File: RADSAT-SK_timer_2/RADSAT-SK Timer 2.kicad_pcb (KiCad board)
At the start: 2 copper layers, 90.2 x 95.9 mm, 70 parts, among them J201 Conn_01x07, J202 Conn_01x05_Female, J203 Conn_01x03, J204 Conn_01x02, J205 Conn_01x02, J206 Conn_01x02, J207 Conn_02x26_Odd_Even, J208 Conn_02x26_Odd_Even, Q204 IRLML2060, Q205 IRLML2060, Q206 IRLML2060, SW201 SW_Push, SW202 SW_Push, SW203 SW_Push, SW204 SW_Push, SW205 SW_Push, SW206 SW_Push, U101 LT1521, U102 Galaxia_Timer, U202 TPS3700DDCR, U230 CPC1114N, U240 CPC1114N, U250 CPC1114N, U260 CPC1114N

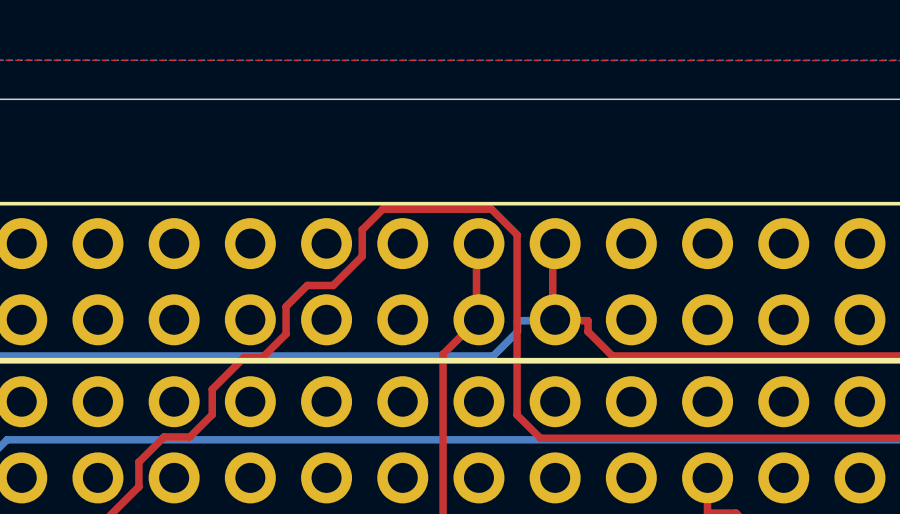
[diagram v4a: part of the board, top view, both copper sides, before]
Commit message: corrected I2C CSKB trace
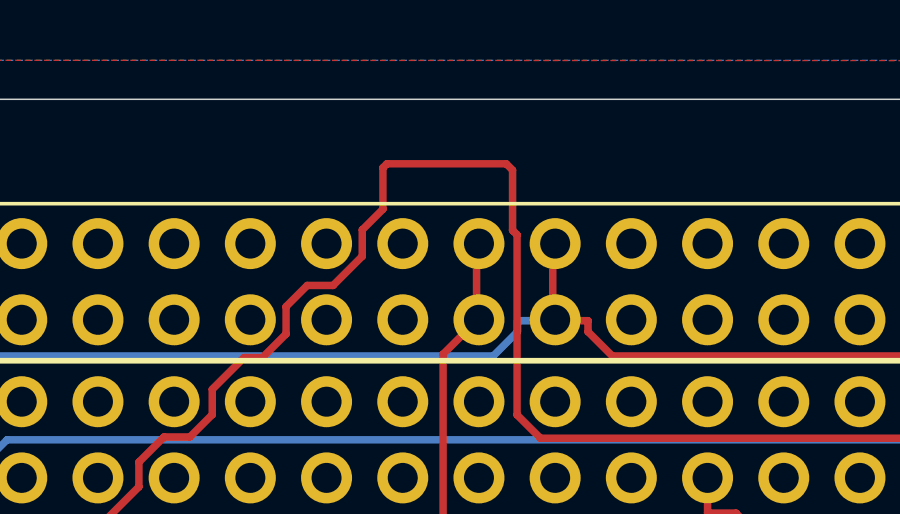
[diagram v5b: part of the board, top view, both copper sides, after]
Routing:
- net I2C_DATA: track 76.4 -> 79.6 mm
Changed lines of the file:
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@@
     (thickness 1.6)
     (drawings 233)
-    (tracks 416)
+    (tracks 421)
     (zones 0)
     (modules 70)
@@
   (segment (start 39.41 71.32) (end 53.0747 71.32) (width 0.25) (layer F.Cu) (net 1))
   (segment (start 53.0747 71.32) (end 53.2747 71.12) (width 0.25) (layer F.Cu) (net 1))
+  (segment (start 80.63 54.5165) (end 80.63 60.5183) (width 0.25) (layer F.Cu) (net 2))
+  (segment (start 80.63 60.5183) (end 81.4097 61.298) (width 0.25) (layer F.Cu) (net 2))
+  (segment (start 81.4097 61.298) (end 98.462 61.298) (width 0.25) (layer F.Cu) (net 2))
+  (segment (start 98.462 61.298) (end 99.68 60.08) (width 0.25) (layer F.Cu) (net 2))
+  (segment (start 56.6674 70.19) (end 57.28 70.19) (width 0.25) (layer F.Cu) (net 2))
+  (segment (start 56.6674 70.19) (end 56.0547 70.19) (width 0.25) (layer F.Cu) (net 2))
+  (segment (start 39.41 70.07) (end 55.9347 70.07) (width 0.25) (layer F.Cu) (net 2))
+  (segment (start 55.9347 70.07) (end 56.0547 70.19) (width 0.25) (layer F.Cu) (net 2))
+  (segment (start 80.27 52.15) (end 80.48 52.36) (width 0.25) (layer F.Cu) (net 2))
+  (segment (start 76.2892 52.15) (end 80.27 52.15) (width 0.25) (layer F.Cu) (net 2))
+  (segment (start 76.1596 52.2796) (end 76.2892 52.15) (width 0.25) (layer F.Cu) (net 2))
+  (segment (start 76.1596 53.6616) (end 76.1596 52.2796) (width 0.25) (layer F.Cu) (net 2))
+  (segment (start 75.47 54.3512) (end 76.1596 53.6616) (width 0.25) (layer F.Cu) (net 2))
+  (segment (start 75.47 55.2342) (end 75.47 54.3512) (width 0.25) (layer F.Cu) (net 2))
+  (segment (start 74.4996 56.2046) (end 75.47 55.2342) (width 0.25) (layer F.Cu) (net 2))
+  (segment (start 72.93 56.9124) (end 73.6378 56.2046) (width 0.25) (layer F.Cu) (net 2))
+  (segment (start 80.52675 54.41325) (end 80.63 54.5165) (width 0.25) (layer F.Cu) (net 2))
+  (segment (start 80.48 52.36) (end 80.48 54.3665) (width 0.25) (layer F.Cu) (net 2))
   (segment (start 57.28 70.19) (end 60.7524 70.19) (width 0.25) (layer F.Cu) (net 2))
+  (segment (start 80.48 54.3665) (end 80.52675 54.41325) (width 0.25) (layer F.Cu) (net 2))
+  (segment (start 73.6378 56.2046) (end 74.4996 56.2046) (width 0.25) (layer F.Cu) (net 2))
   (segment (start 60.7524 70.19) (end 68.0246 62.9178) (width 0.25) (layer F.Cu) (net 2))
+  (segment (start 70.47 60.511) (end 70.47 59.669) (width 0.25) (layer F.Cu) (net 2))
   (segment (start 68.0246 62.9178) (end 68.0246 62.0944) (width 0.25) (layer F.Cu) (net 2))
   (segment (start 68.0246 62.0944) (end 68.8636 61.2554) (width 0.25) (layer F.Cu) (net 2))
   (segment (start 68.8636 61.2554) (end 69.7256 61.2554) (width 0.25) (layer F.Cu) (net 2))
   (segment (start 69.7256 61.2554) (end 70.47 60.511) (width 0.25) (layer F.Cu) (net 2))
-  (segment (start 70.47 60.511) (end 70.47 59.669) (width 0.25) (layer F.Cu) (net 2))
   (segment (start 70.47 59.669) (end 71.528 58.611) (width 0.25) (layer F.Cu) (net 2))
   (segment (start 71.528 58.611) (end 72.1415 58.611) (width 0.25) (layer F.Cu) (net 2))
   (segment (start 72.1415 58.611) (end 72.93 57.8225) (width 0.25) (layer F.Cu) (net 2))
   (segment (start 72.93 57.8225) (end 72.93 56.9124) (width 0.25) (layer F.Cu) (net 2))
-  (segment (start 72.93 56.9124) (end 73.6378 56.2046) (width 0.25) (layer F.Cu) (net 2))
-  (segment (start 73.6378 56.2046) (end 74.4996 56.2046) (width 0.25) (layer F.Cu) (net 2))
-  (segment (start 74.4996 56.2046) (end 75.47 55.2342) (width 0.25) (layer F.Cu) (net 2))
-  (segment (start 75.47 55.2342) (end 75.47 54.3512) (width 0.25) (layer F.Cu) (net 2))
-  (segment (start 75.47 54.3512) (end 76.1596 53.6616) (width 0.25) (layer F.Cu) (net 2))
-  (segment (start 76.1596 53.6616) (end 79.7751 53.6616) (width 0.25) (layer F.Cu) (net 2))
-  (segment (start 79.7751 53.6616) (end 80.63 54.5165) (width 0.25) (layer F.Cu) (net 2))
-  (segment (start 80.63 54.5165) (end 80.63 60.5183) (width 0.25) (layer F.Cu) (net 2))
-  (segment (start 80.63 60.5183) (end 81.4097 61.298) (width 0.25) (layer F.Cu) (net 2))
-  (segment (start 81.4097 61.298) (end 98.462 61.298) (width 0.25) (layer F.Cu) (net 2))
-  (segment (start 98.462 61.298) (end 99.68 60.08) (width 0.25) (layer F.Cu) (net 2))
-  (segment (start 56.6674 70.19) (end 57.28 70.19) (width 0.25) (layer F.Cu) (net 2))
-  (segment (start 56.6674 70.19) (end 56.0547 70.19) (width 0.25) (layer F.Cu) (net 2))
-  (segment (start 39.41 70.07) (end 55.9347 70.07) (width 0.25) (layer F.Cu) (net 2))
-  (segment (start 55.9347 70.07) (end 56.0547 70.19) (width 0.25) (layer F.Cu) (net 2))
   (segment (start 119.708 97.4) (end 117.186 97.4) (width 0.25) (layer F.Cu) (net 4))
   (segment (start 117.186 97.4) (end 116.288 98.298) (width 0.25) (layer F.Cu) (net 4))

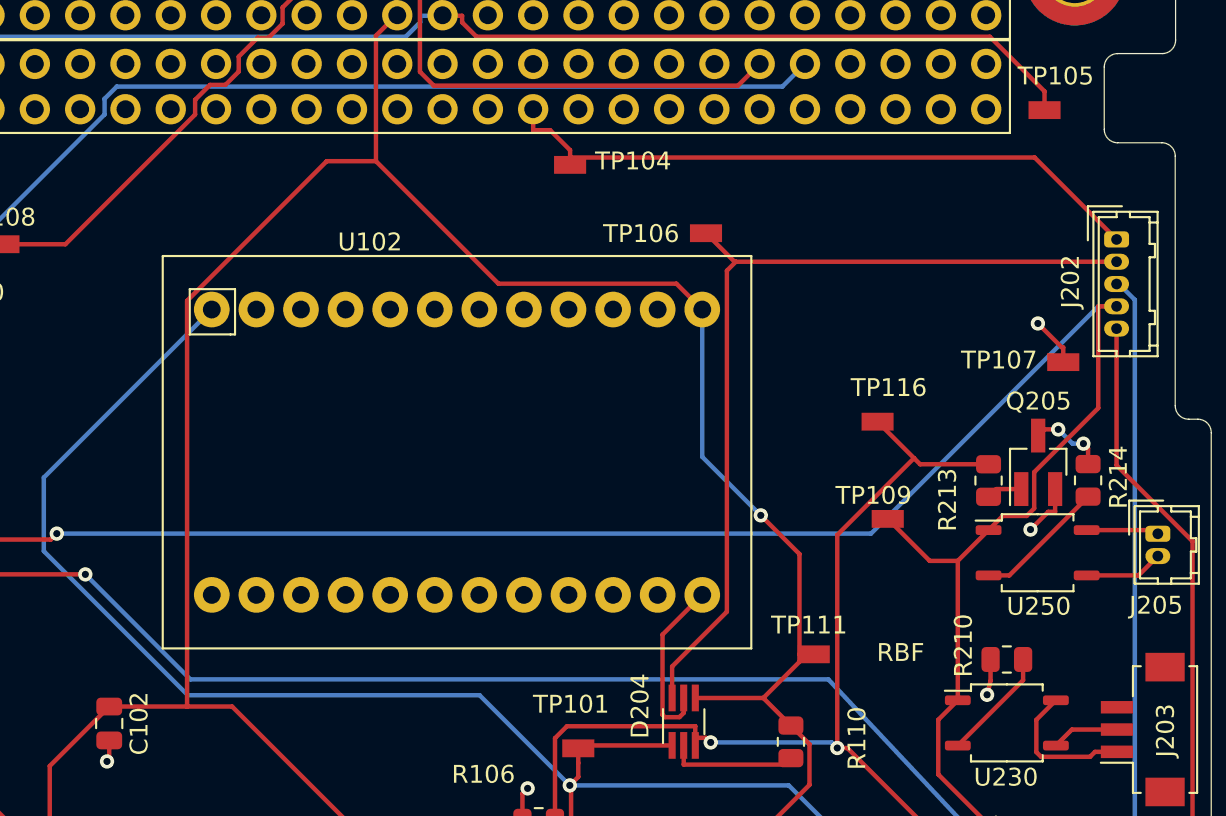
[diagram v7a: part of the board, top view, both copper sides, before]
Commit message: gave traces breathing room along the galaxia timer
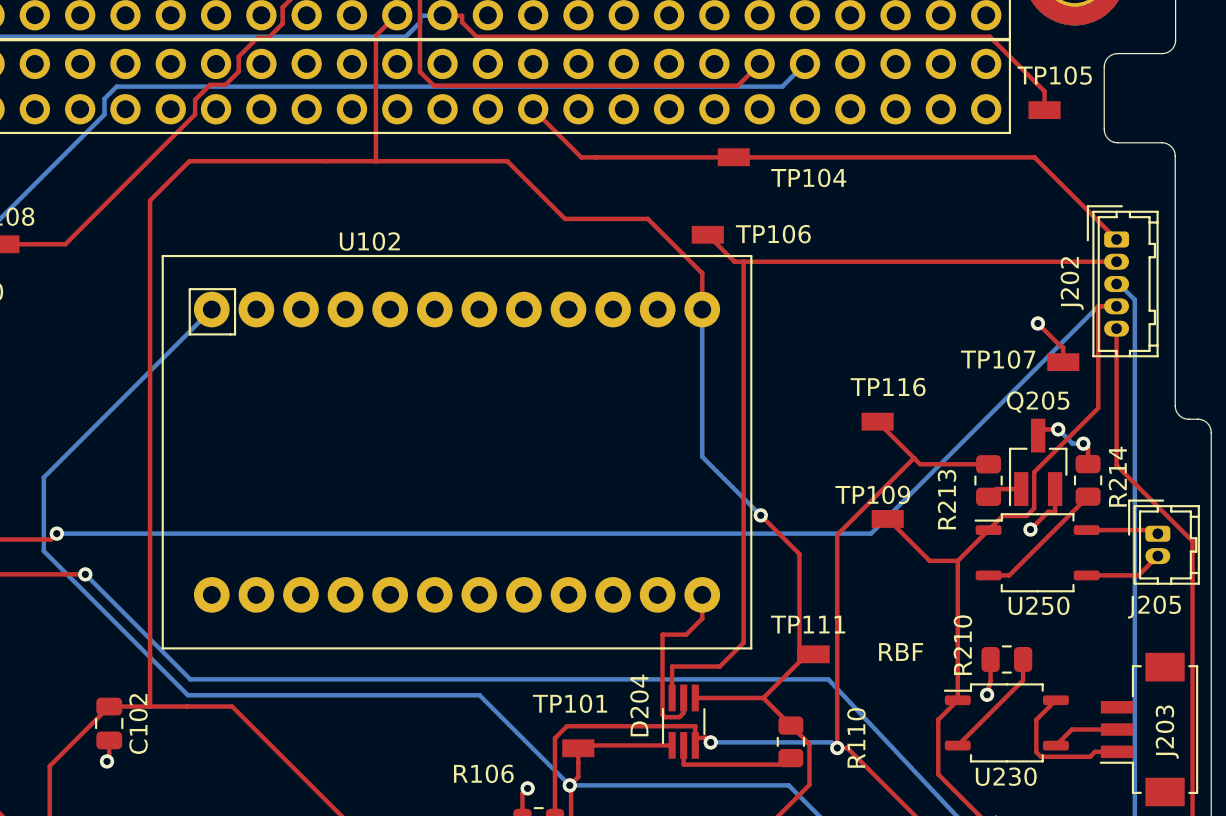
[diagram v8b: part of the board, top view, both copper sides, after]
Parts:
- moved TP104 9.19 mm to (98.2, 65.3)
- moved TP106 0.13 mm to (96.8, 69.7)
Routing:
- net +5V: track 149.6 -> 156.2 mm
- net Net-(D204-Pad6): track 49.6 -> 51.4 mm
- net Inhib_EN: track 9.83 -> 10.6 mm
- net USB_Charge: track 37.1 -> 36.4 mm
